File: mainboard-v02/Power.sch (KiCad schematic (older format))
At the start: 36 parts, among them Q1 IRLML2803, U4 MAX4372TEUK+T, U5 TPS54226PWPRPWP14_2P31X2P46-L, U6 LTC4121, U7 NDS8434

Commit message: fixing bold font and adding schematic pdf of v02
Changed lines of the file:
@@
 EESchema Schematic File Version 4
-LIBS:mainboard
 EELAYER 29 0
 EELAYER END
@@
 Wire Wire Line
 	3600 2800 3600 2900
-Text GLabel 3600 2800 0    10   BiDi ~ 0
+Text GLabel 3600 2800 0    10   BiDi ~ 2
 GND
 Wire Wire Line
@@
 	6900 3300 7200 3300
 Connection ~ 7200 3300
-Text GLabel 7200 3300 0    10   BiDi ~ 0
+Text GLabel 7200 3300 0    10   BiDi ~ 2
 GND
 Wire Wire Line
 	8100 2500 7900 2500
-Text GLabel 8100 2500 0    10   BiDi ~ 0
+Text GLabel 8100 2500 0    10   BiDi ~ 2
 GND
 Wire Wire Line
 	3300 1400 3500 1400
-Text GLabel 3300 1400 0    10   BiDi ~ 0
+Text GLabel 3300 1400 0    10   BiDi ~ 2
 GND
 Wire Wire Line
 	3900 2800 3900 2900
-Text GLabel 3900 2800 0    10   BiDi ~ 0
+Text GLabel 3900 2800 0    10   BiDi ~ 2
 GND
 Wire Wire Line
@@
 Connection ~ 5700 2700
 Connection ~ 5700 2900
-Text GLabel 5600 2500 0    10   BiDi ~ 0
+Text GLabel 5600 2500 0    10   BiDi ~ 2
 GND
 Wire Wire Line
@@
 	3200 5400 3900 5400
 Connection ~ 3900 5400
-Text GLabel 3900 5500 0    10   BiDi ~ 0
+Text GLabel 3900 5500 0    10   BiDi ~ 2
 GND
 Wire Wire Line
@@
 Connection ~ 6100 6400
 Connection ~ 6300 7100
-Text GLabel 6100 7100 0    10   BiDi ~ 0
+Text GLabel 6100 7100 0    10   BiDi ~ 2
 GND
 Wire Wire Line
@@
 Connection ~ 2900 6900
 Connection ~ 2300 6900
-Text GLabel 2900 6700 0    10   BiDi ~ 0
+Text GLabel 2900 6700 0    10   BiDi ~ 2
 GND
 Wire Wire Line
@@
 Connection ~ 1900 5800
 Connection ~ 2400 5800
-Text GLabel 2900 6000 0    10   BiDi ~ 0
+Text GLabel 2900 6000 0    10   BiDi ~ 2
 GND
 Wire Wire Line
 	8650 6200 7950 6200
 Connection ~ 7950 6200
-Text GLabel 8650 6200 0    10   BiDi ~ 0
+Text GLabel 8650 6200 0    10   BiDi ~ 2
 GND
 Wire Wire Line
@@
 	3900 4900 3900 5000
 Connection ~ 3900 5000
-Text GLabel 3900 5100 0    10   BiDi ~ 0
+Text GLabel 3900 5100 0    10   BiDi ~ 2
 3.3V
 Wire Wire Line
@@
 Connection ~ 1600 6100
 Connection ~ 1900 6100
-Text GLabel 1400 5800 0    10   BiDi ~ 0
+Text GLabel 1400 5800 0    10   BiDi ~ 2
 3.3V
 Wire Wire Line
@@
 	7750 1500 7750 1600
 Connection ~ 7750 1500
-Text GLabel 7300 1600 0    10   BiDi ~ 0
+Text GLabel 7300 1600 0    10   BiDi ~ 2
 3.3V
 Wire Wire Line
@@
 Wire Wire Line
 	3300 2300 3200 2300
-Text GLabel 3200 2300 0    70   BiDi ~ 0
+Text GLabel 3200 2300 0    70   BiDi ~ 14
 VSOLAR
 Wire Wire Line
@@
 Wire Wire Line
 	7000 2300 7100 2300
-Text GLabel 8900 2800 2    70   BiDi ~ 0
+Text GLabel 8900 2800 2    70   BiDi ~ 14
 VBATT
 Wire Wire Line
@@
 Text Notes 2100 4800 0    59   ~ 0
 Battery Current Sensor
-Text Notes 8550 4900 0    85   ~ 0
+Text Notes 8550 4900 0    85   ~ 17
 GPS Power
-Text Notes 4200 1000 0    85   ~ 0
+Text Notes 4200 1000 0    85   ~ 17
 2s2P Li-Ion Battery Charging Circuit
-Text Notes 2800 4400 0    85   ~ 0
+Text Notes 2800 4400 0    85   ~ 17
 Regulator - 3.3V OUT
-Text Notes 1200 6300 0    42   ~ 0
+Text Notes 1900 6500 2    42   ~ 8
 VBATT 4.5 to 18V
 Text Notes 8300 2200 0    59   ~ 0
@@
 Wire Wire Line
 	10300 5800 10500 5800
-Connection ~ 10300 5800
-Connection ~ 10300 5400
 Wire Wire Line
 	10300 5400 10300 5600
-Connection ~ 10300 5600
 Wire Wire Line
 	10300 5600 10300 5800
@@
 	1    0    0    -1
 $EndComp
-Text Notes 3600 1150 0    85   ~ 0
+Text Notes 3600 1150 0    85   ~ 17
 DNI
 Text GLabel 7400 2050 2    50   Output ~ 0

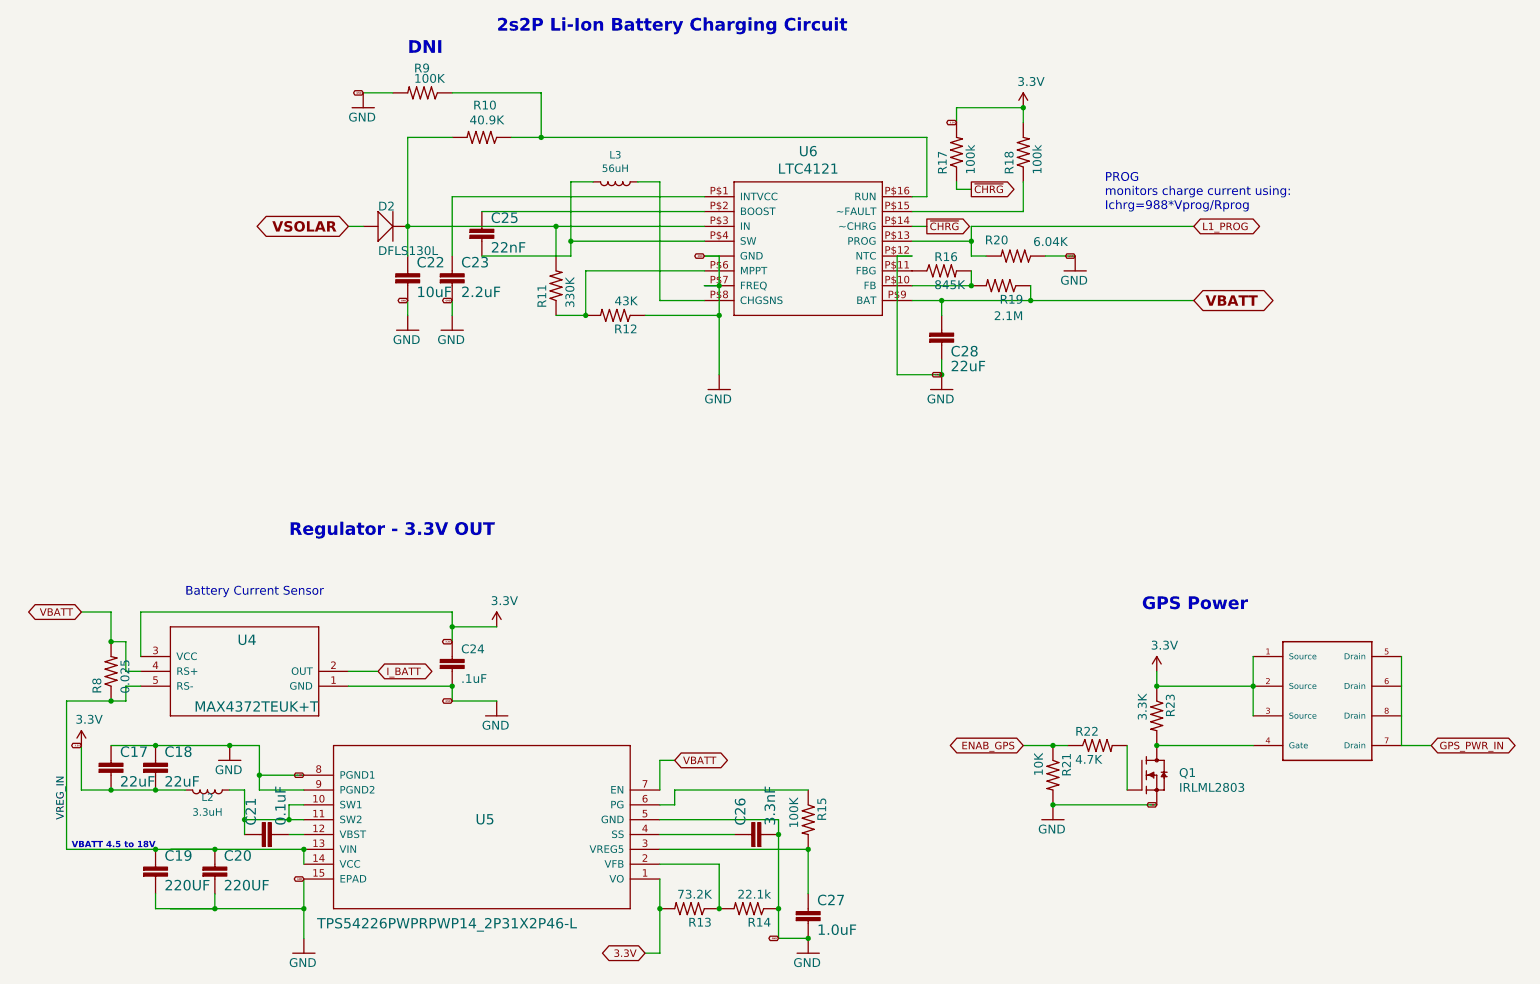
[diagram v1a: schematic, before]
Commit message: mainboard-v02 with RFM98PW
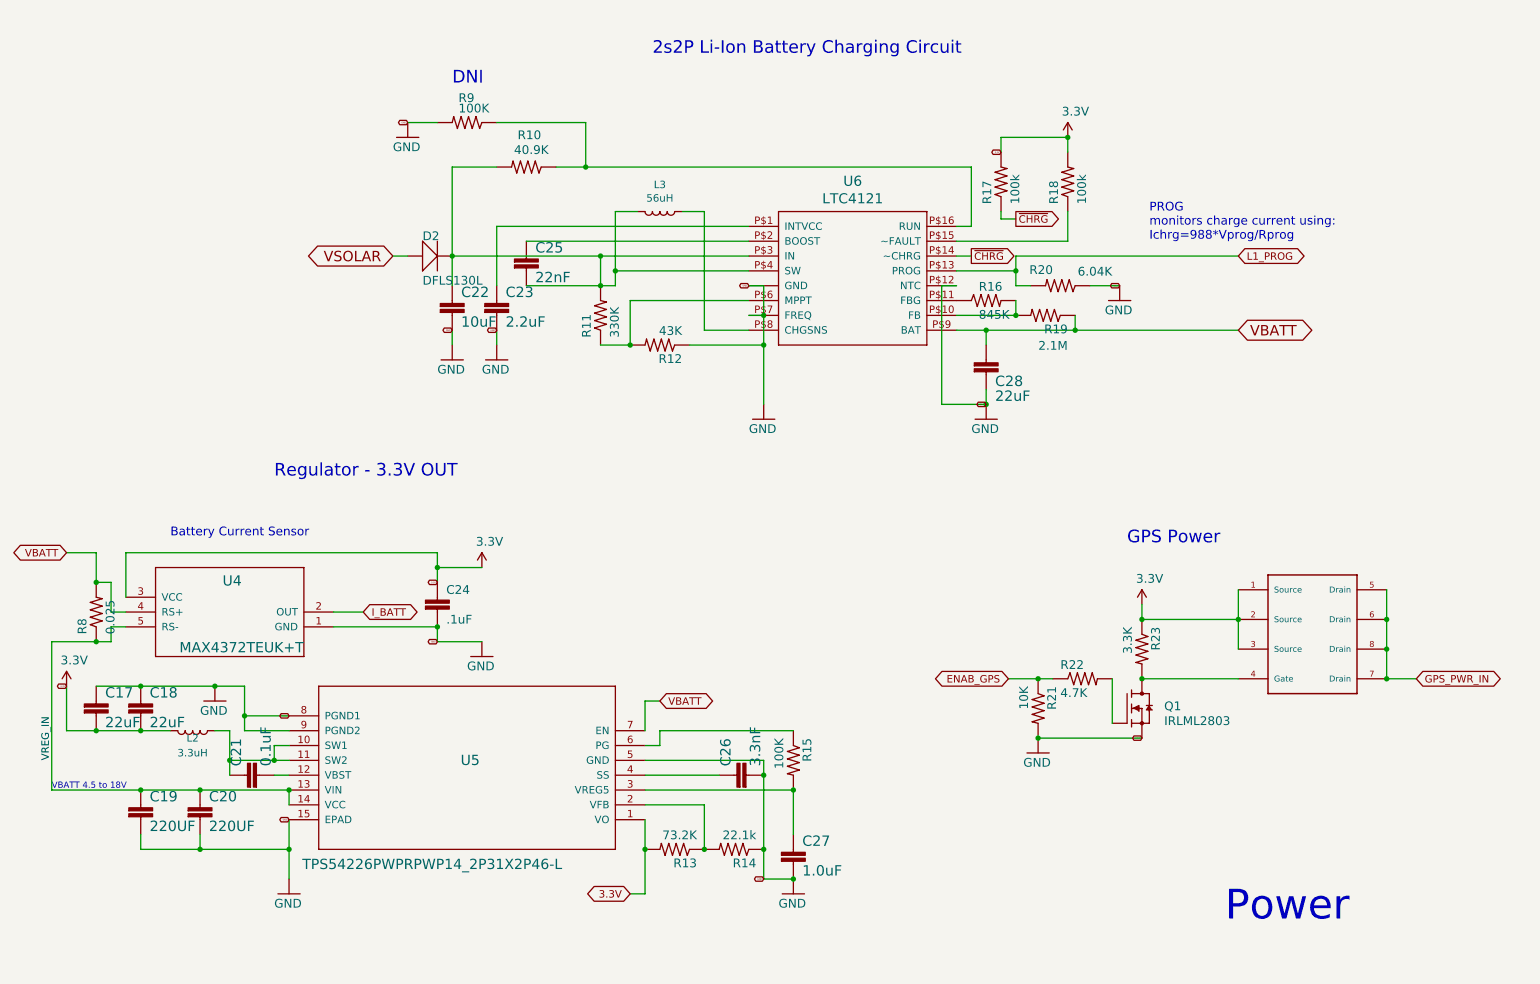
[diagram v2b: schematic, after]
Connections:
- net at C25.2, L3.2, U6.P$4 (SW): now also C22.1, D2.C, R10.2, R11.2, U6.P$3 (IN)
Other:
- note added: "Power"
- moved on the sheet: C17, C18, C19, C20, C21, C22, C23, C24, C25, C26, C27, C28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
